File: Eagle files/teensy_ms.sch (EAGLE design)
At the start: 14 parts, among them IC1 SN65HVD230, IC2 TEENSY_3.0_BASIC-MIN

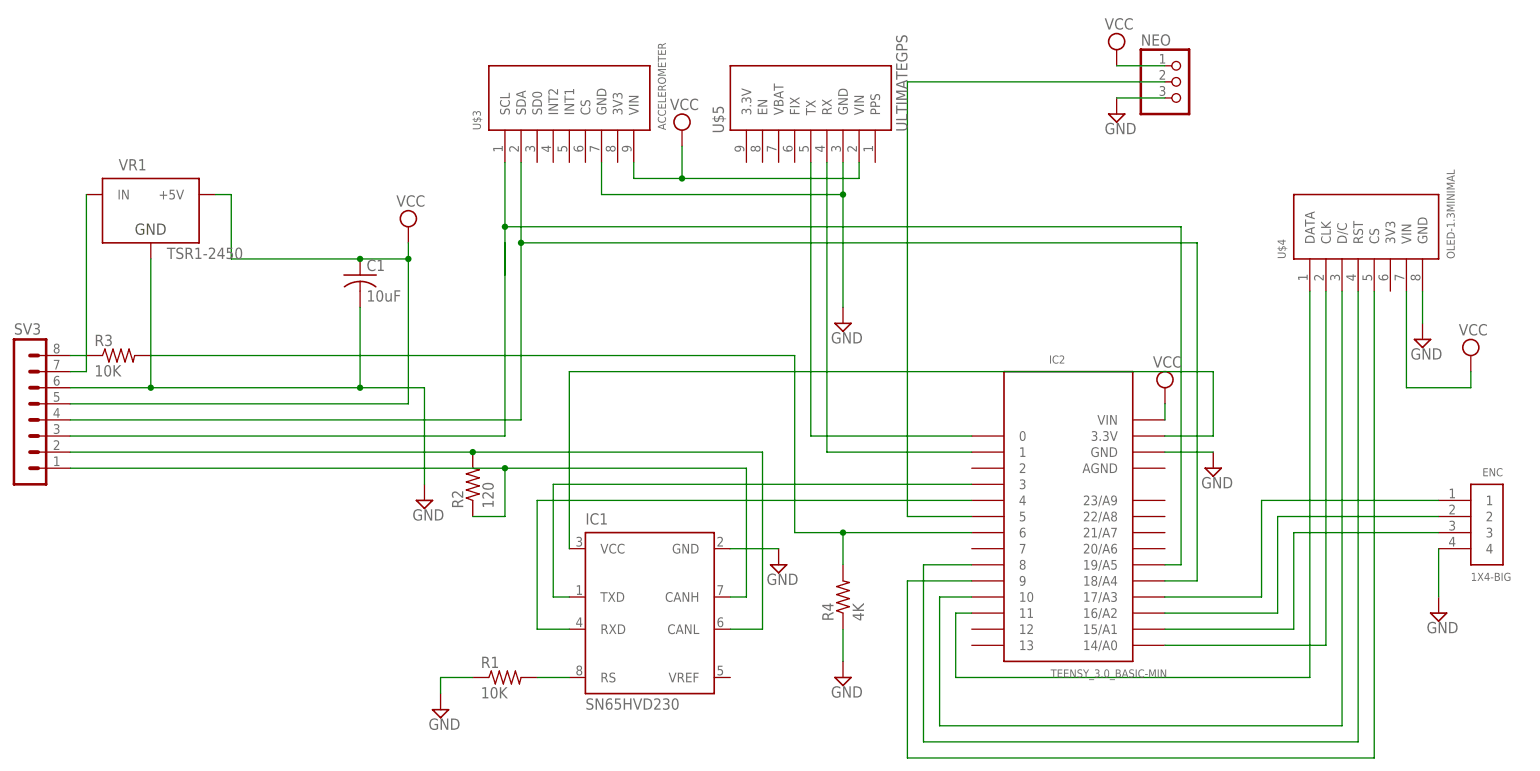
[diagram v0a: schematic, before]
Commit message: Remove GPS and Accel from PCB
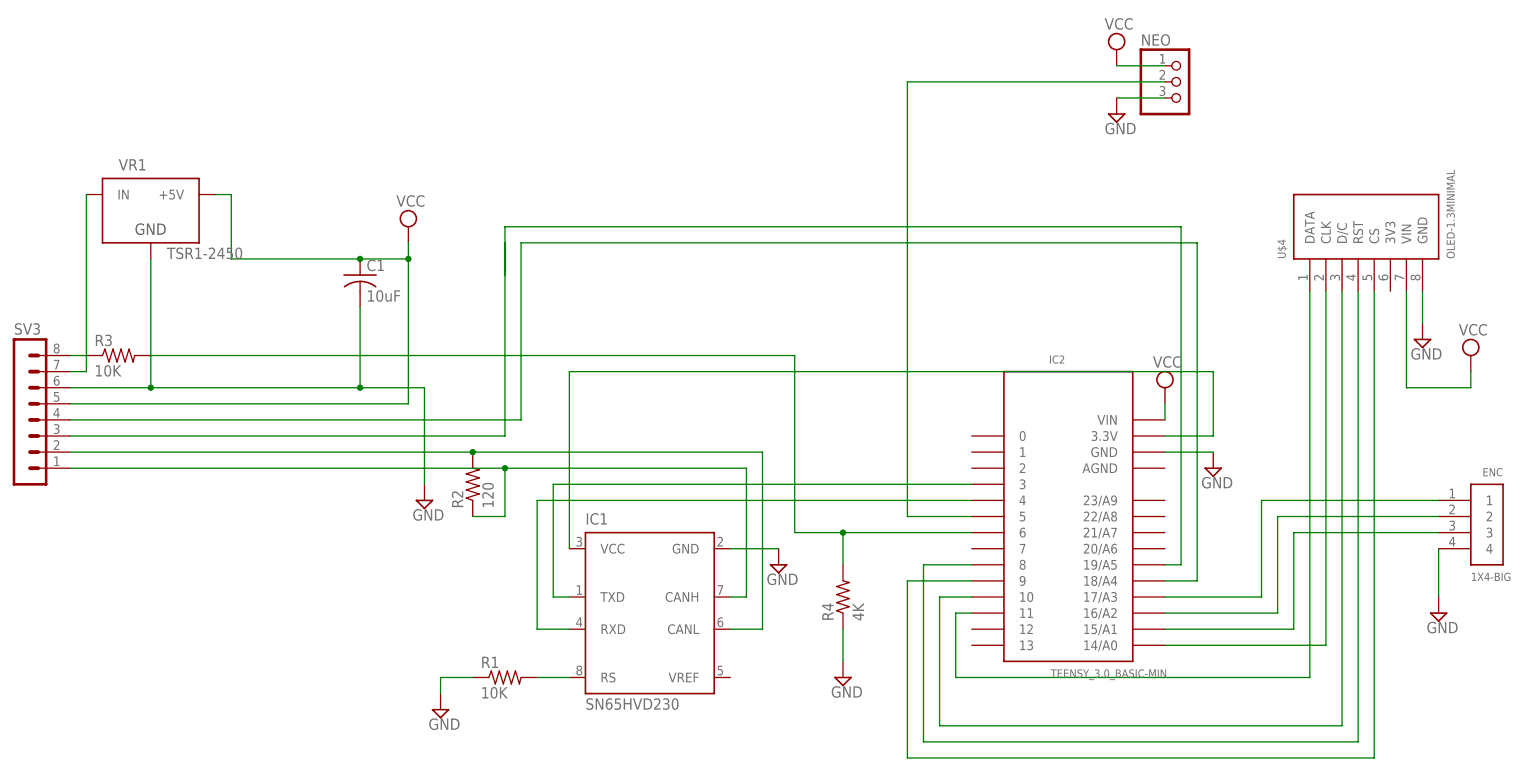
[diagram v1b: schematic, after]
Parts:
- removed U$3: ACCELEROMETER, custom:ACCELEROMETER
- removed U$5: ULTIMATEGPS, custom:ULTIMATEGPS
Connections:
- removed net N$4: IC2.1, U$5.RX
- removed net N$5: IC2.0, U$5.TX
- net GND: no longer U$3.GND, U$5.GND
- net N$14: no longer U$3.SCL
- net N$16: no longer U$3.SDA
- net VCC: no longer U$3.VIN, U$5.VIN
